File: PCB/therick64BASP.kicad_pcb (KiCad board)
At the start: 2 copper layers, 312.4 x 75.8 mm, 165 parts, among them J1 TYPE-C-31-M12_13, J2 AVR-ISP-6, K1 KEYSW, K10 KEYSW, K11 KEYSW, K12 KEYSW, K13 KEYSW, K14 KEYSW, K15 KEYSW, K16 KEYSW, K17 KEYSW, K18 KEYSW, K19 KEYSW, K2 KEYSW, K20 KEYSW, K21 KEYSW, K22 KEYSW, K23 KEYSW, K24 KEYSW, K25 KEYSW, K26 KEYSW, K27 KEYSW, K28 KEYSW, K29 KEYSW, K3 KEYSW, K30 KEYSW, K31 KEYSW, K32 KEYSW, K33 KEYSW, K34 KEYSW, K35 KEYSW, K36 KEYSW, K37 KEYSW, K38 KEYSW, K39 KEYSW, K4 KEYSW, K40 KEYSW, K41 KEYSW, K42 KEYSW, K43 KEYSW, K44 KEYSW, K45 KEYSW, K46 KEYSW, K47 KEYSW, K48 KEYSW, K49 KEYSW, K5 KEYSW, K50 KEYSW, K51 KEYSW, K52 KEYSW, K53 KEYSW, K54 KEYSW, K55 KEYSW, K56 KEYSW, K57 KEYSW, K58 KEYSW, K59 KEYSW, K6 KEYSW, K60 KEYSW, K61 KEYSW, K62 KEYSW, K63 KEYSW, K64 KEYSW, K7 KEYSW, K8 KEYSW, K9 KEYSW, SW1 SW_PUSH, U1 ATMEGA32U4, U2 HOLE, U3 USBLC6-2SC6, U4 HOLE, U5 HOLE, U6 HOLE, U7 HOLE, U8 HOLE, Y1 16MHz

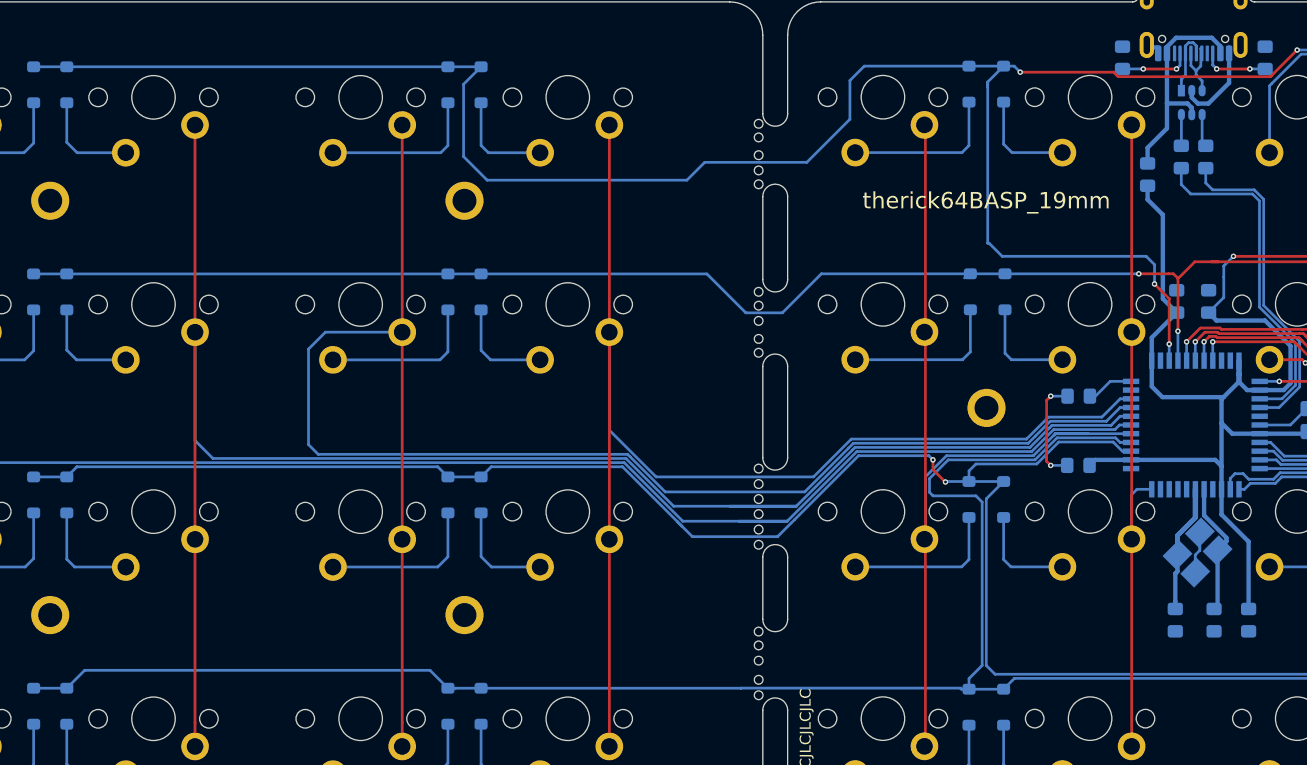
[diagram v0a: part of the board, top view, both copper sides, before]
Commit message: Update some routing
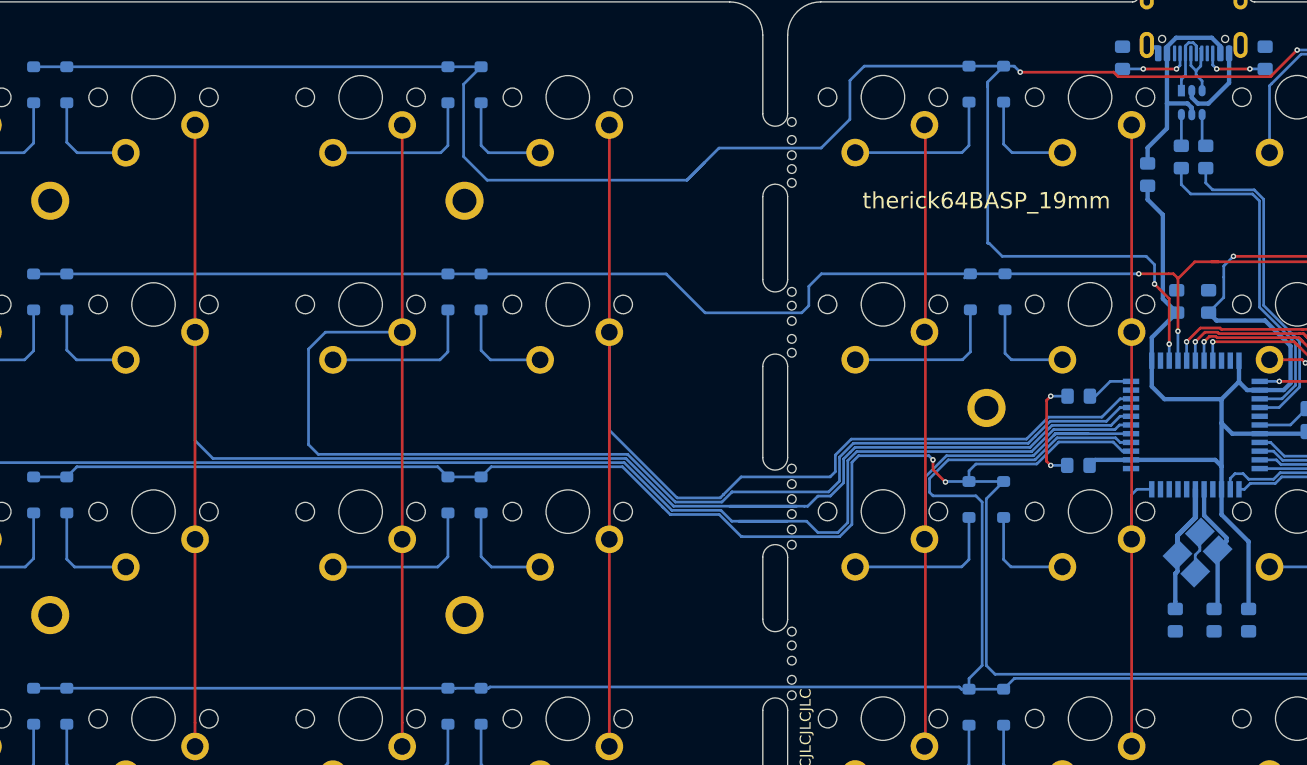
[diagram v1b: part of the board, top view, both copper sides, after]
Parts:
- moved U8 87.9 mm to (284.6, 101.8)
- moved U4 3.04 mm to (136.0, 58.5)
- moved U5 3.04 mm to (136.0, 104.9)
- moved U6 3.04 mm to (136.0, 73.7)
- moved U7 3.04 mm to (136.0, 90.1)
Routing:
- net col12: track 200.4 -> 204.6 mm
- net row2: track 431.2 -> 433.9 mm
- net col15: track 118.6 -> 121.1 mm
- net row0: track 341.7 -> 344.0 mm
- net col14: track 155.4 -> 157.5 mm
- net VCC: track 146.7 -> 144.7 mm
- net col13: track 164.8 -> 166.1 mm
- net row3: track 328.8 -> 327.5 mm
- net row1: track 293.1 -> 294.2 mm

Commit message: Align Switches
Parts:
- moved K61 0.87 mm to (58.9, 109.4)
- moved K62 0.87 mm to (77.9, 109.4)
- moved K57 0.87 mm to (58.9, 90.4)
- moved K63 0.87 mm to (96.9, 109.4)
- moved K64 0.87 mm to (115.9, 109.4)
- moved K53 0.87 mm to (58.9, 71.4)
- moved K59 0.87 mm to (96.9, 90.4)
- moved K54 0.87 mm to (77.9, 71.4)
- moved K60 0.87 mm to (115.9, 90.4)
- moved K49 0.87 mm to (58.9, 52.4)
- moved K55 0.87 mm to (96.9, 71.4)
- moved K50 0.87 mm to (77.9, 52.4)
- moved K56 0.87 mm to (115.9, 71.4)
- moved K51 0.87 mm to (96.9, 52.4)
- moved K52 0.87 mm to (115.9, 52.4)
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
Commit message: Changed pins to make routing cleaner
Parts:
- removed U8: HOLE, Artwork:QMKBadgeSmall
- moved D37 0.89 mm to (152.7, 107.5)
- moved D38 0.89 mm to (155.8, 107.5)
- moved D39 0.89 mm to (190.6, 107.5)
- moved D40 0.89 mm to (193.8, 107.5)
- moved D41 0.89 mm to (228.6, 107.5)
- moved D42 0.89 mm to (231.8, 107.5)
- moved D43 0.89 mm to (266.7, 107.5)
- moved D44 0.89 mm to (269.9, 107.5)
- moved D45 0.89 mm to (304.7, 107.5)
- moved D46 0.89 mm to (307.9, 107.5)
- moved D47 0.89 mm to (342.7, 107.5)
- moved D48 0.89 mm to (345.8, 107.5)
- moved D61 0.76 mm to (66.9, 107.5)
- moved D62 0.76 mm to (69.9, 107.5)
- moved D63 0.76 mm to (104.9, 107.5)
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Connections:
- U1 pad 10: col4 -> col10
- U1 pad 11: col3 -> col11
- U1 pad 38: col11 -> col3
- U1 pad 39: col10 -> col4
- U1 pad 40: col9 -> col5
- U1 pad 41: col8 -> col6
- U1 pad 8: col6 -> col8
- U1 pad 9: col5 -> col9
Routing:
- net row2: track 433.9 -> 342.7 mm
- net col12: track 204.6 -> 178.2 mm
- net col14: track 157.5 -> 175.7 mm
- net col10: track 238.3 -> 221.5 mm, vias 2 -> 0
- net col8: track 198.7 -> 183.5 mm, vias 2 -> 0
- net col11: track 256.7 -> 242.2 mm, vias 2 -> 0
- net col9: track 218.1 -> 205.1 mm, vias 2 -> 0
- net VCC: track 144.7 -> 152.5 mm, vias 2 -> 6
- net col13: track 166.1 -> 159.6 mm
- net col7: track 171.7 -> 165.8 mm
- net XTAL2: track 18.4 -> 13.2 mm
- net col2: track 79.4 -> 74.7 mm
- net row3: track 327.5 -> 323.7 mm
- net col0: track 86.7 -> 83.5 mm
- net col3: track 104.6 -> 107.2 mm, vias 0 -> 2
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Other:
- outline, holes or cut-outs redrawn
- board text added: "PCB Rev 1.0"
- board text added: "therick64BASP"
- board text removed: "therick"
- board text removed: "therick64BASP_19mm"

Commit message: Remapped ISP Flash, added mounting holes
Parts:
- added H11: MountingHole, random-keyboard-parts:plate_hole_4mm_tht, F.Cu at (154.3, 64.0)
- added H12: MountingHole, random-keyboard-parts:plate_hole_4mm_tht, F.Cu at (154.3, 102.0)
- added H13: MountingHole, random-keyboard-parts:plate_hole_4mm_tht, F.Cu at (287.2, 102.0)
- added H14: MountingHole, random-keyboard-parts:plate_hole_4mm_tht, F.Cu at (211.2, 102.0)
- added H15: MountingHole, random-keyboard-parts:plate_hole_4mm_tht, F.Cu at (211.2, 64.0)
- added H16: MountingHole, random-keyboard-parts:plate_hole_4mm_tht, F.Cu at (287.2, 64.0)
- added H17: MountingHole, random-keyboard-parts:plate_hole_4mm_tht, F.Cu at (344.2, 102.0)
- added H18: MountingHole, random-keyboard-parts:plate_hole_4mm_tht, F.Cu at (344.2, 64.0)
- H1, H10, H2, H3, H4, H5, H6, H7, H8, H9: footprint random-keyboard-parts:Generic-Mounthole -> random-keyboard-parts:plate_hole_4mm_tht
- J2: value AVR-ISP-6 -> AVR-ISP-6_mod
- moved J2 38.1 mm to (249.1, 61.7)
- moved H2 2.03 mm to (192.2, 64.0)
- moved H7 2.03 mm to (68.3, 64.0)
- moved H4 2.03 mm to (306.2, 64.0)
- moved H10 2.03 mm to (106.3, 102.0)
- moved H9 2.03 mm to (68.3, 102.0)
- moved H8 2.03 mm to (106.4, 64.0)
- moved H1 2.03 mm to (154.3, 83.0)
- moved H3 2.01 mm to (192.2, 102.0)
- moved H5 2.01 mm to (306.2, 102.0)
- moved H6 2.01 mm to (344.2, 83.0)
- moved D10 0.51 mm to (307.9, 50.2)
- moved D11 0.51 mm to (342.7, 50.2)
- moved D12 0.51 mm to (345.8, 50.2)
- moved D5 0.51 mm to (228.7, 50.2)
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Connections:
- J2 pad 1: col3 -> ISP_Reset
- J2 pad 3: col5 -> col11
- J2 pad 4: col4 -> col10
- J2 pad 5: ISP_Reset -> col9
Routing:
- net col11: track 242.2 -> 376.0 mm, vias 0 -> 1
- net col10: track 221.5 -> 337.1 mm
- net col9: track 205.1 -> 295.2 mm
- net VCC: track 152.5 -> 216.9 mm, vias 6 -> 7
- net col5: track 176.4 -> 135.4 mm
- net ISP_Reset: track 64.9 -> 105.1 mm
- net col4: track 128.7 -> 114.6 mm
- net Net-(D4-Pad2): track 22.5 -> 18.9 mm
- net row1: track 294.6 -> 296.4 mm
- net row3: track 323.7 -> 324.7 mm
- net row0: track 343.3 -> 342.6 mm
- net Net-(D9-Pad2): track 15.2 -> 15.7 mm
- net Net-(D8-Pad2): track 10.0 -> 10.5 mm
- net Net-(D7-Pad2): track 15.2 -> 15.7 mm
- net Net-(D6-Pad2): track 10.0 -> 10.5 mm
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
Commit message: Added mounting holes
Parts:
- added U8: HOLE, Artwork:THERICK, F.Cu at (249.3, 80.9)
- H1, H10, H11, H12, H13, H14, H15, H16, H17, H18, H2, H3, H4, H5, H6, H7, H8, H9: footprint random-keyboard-parts:plate_hole_4mm_tht -> random-keyboard-parts:Generic-Mounthole
- moved H15 2.03 mm to (211.3, 61.9)
- moved H2 2.03 mm to (192.3, 61.9)
- moved H7 2.03 mm to (68.4, 61.9)
- moved H16 2.03 mm to (287.3, 61.9)
- moved H18 2.03 mm to (344.3, 61.9)
- moved H4 2.03 mm to (306.3, 61.9)
- moved H10 2.03 mm to (106.4, 99.9)
- moved H14 2.03 mm to (211.3, 99.9)
- moved H3 2.03 mm to (192.3, 99.9)
- moved H9 2.03 mm to (68.4, 99.9)
- moved H13 2.03 mm to (287.3, 99.9)
- moved H17 2.03 mm to (344.3, 99.9)
- moved H5 2.03 mm to (306.3, 99.9)
- moved H6 2.03 mm to (344.3, 80.9)
- moved H11 2.03 mm to (154.3, 61.9)
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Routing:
- net col3: track 107.2 -> 99.0 mm
